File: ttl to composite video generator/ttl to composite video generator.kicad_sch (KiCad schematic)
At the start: 29 parts, among them J1 composite video, J10 ground if unused, J11 ground if unused, J12 power in, J2 video in, J3 video polarity, J4 Hsync polarity, J5 Vsync polarity, J6 Hsync in, J7 Vsync in, J8 ground if unused, J9 ground if unused, Q1 PN2222A, U1 74LS86, U2 L7805, U3 74LS04

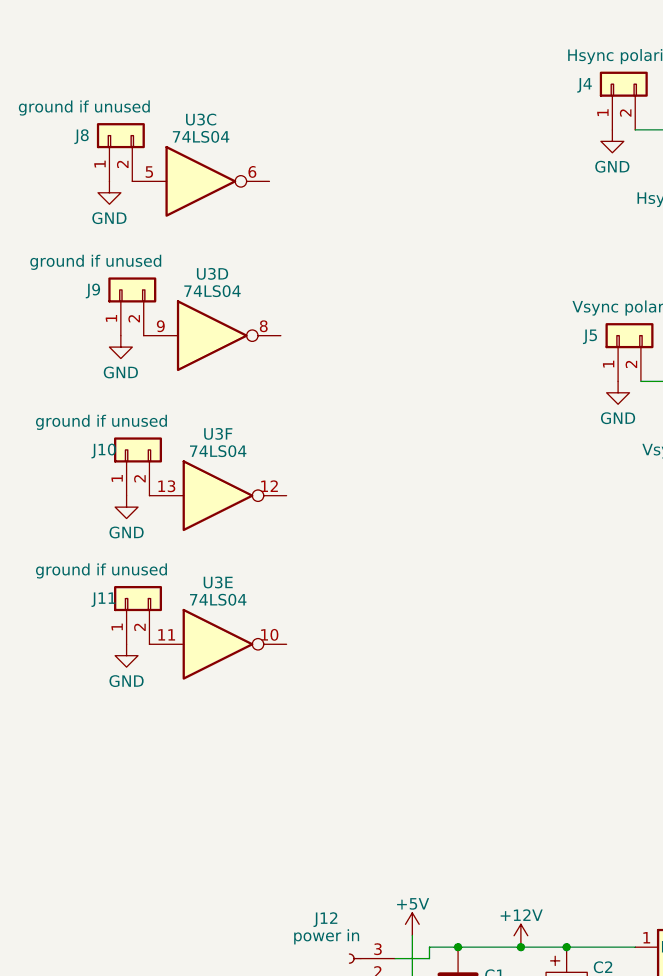
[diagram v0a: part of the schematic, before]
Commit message: added data for board production
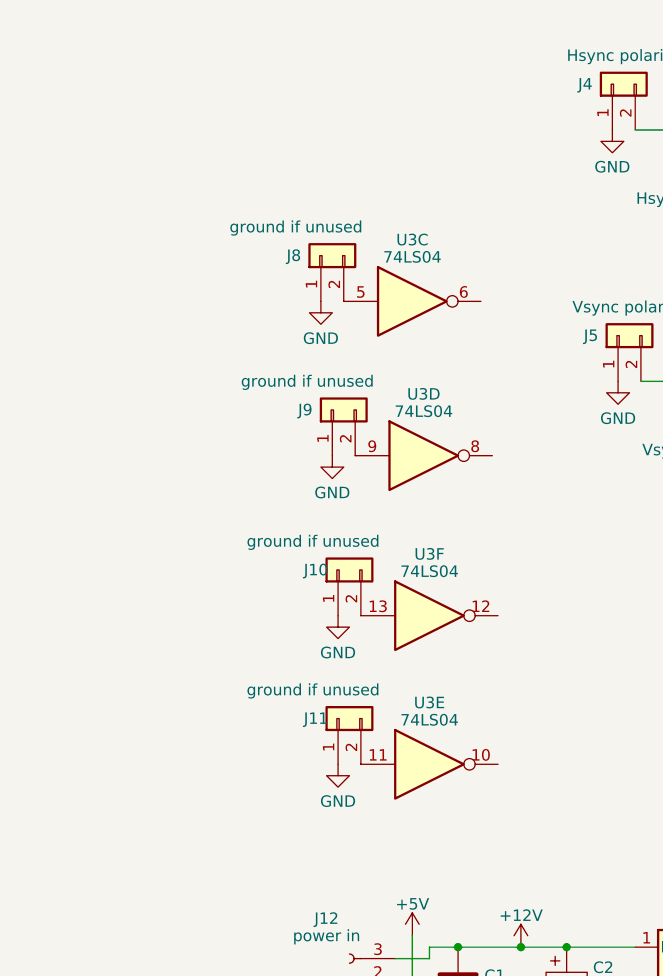
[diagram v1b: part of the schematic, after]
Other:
- moved on the sheet: J10, J11, J8, J9, U3C, U3D, U3E, U3F
